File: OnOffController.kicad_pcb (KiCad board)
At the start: 2 copper layers, 16.3 x 26.4 mm, 35 parts, among them J1 S2B-PH-K-SLFSN, J2 Conn_01x02_Pin, J3 Conn_01x04_Pin, J4 Conn_01x04_Pin, J8 47589-0001, SW1 KMR211GLFS, U1 STM6601, U2 MCP73831-2-OT, U3 SPX3819M5-L

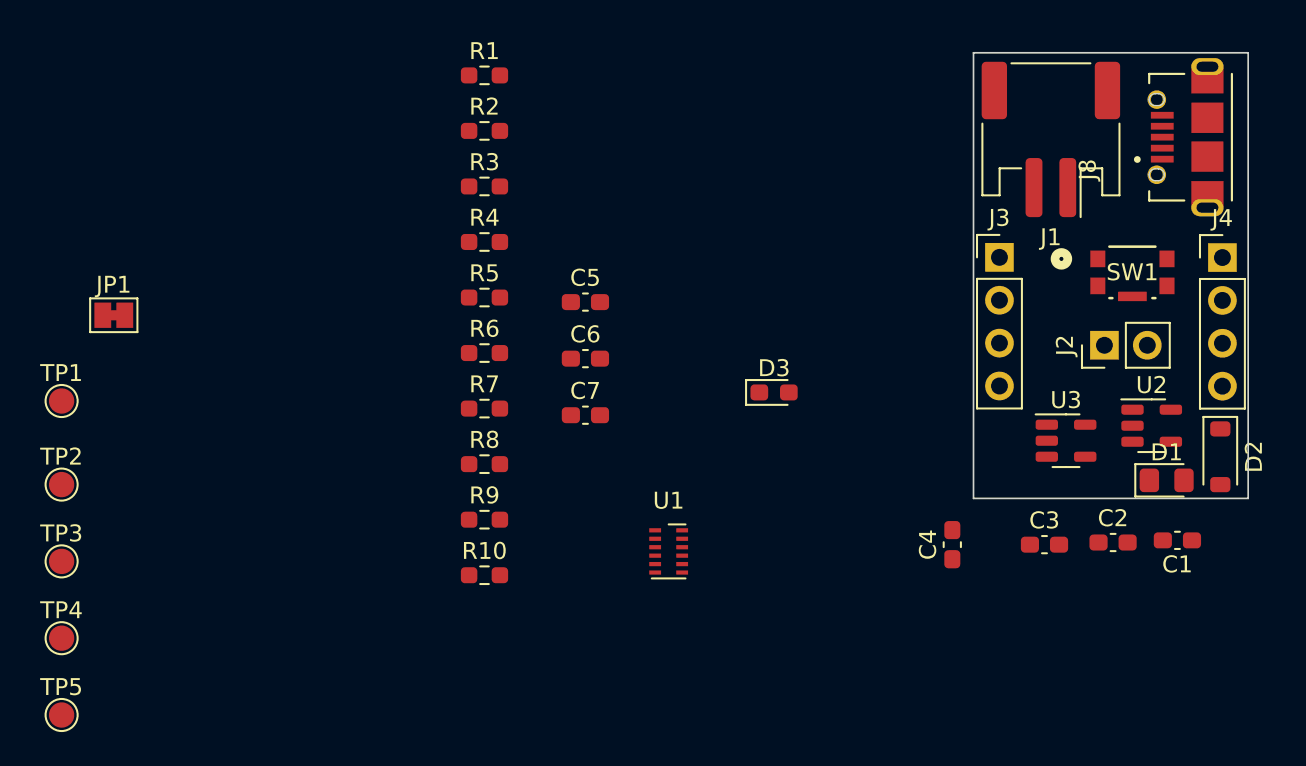
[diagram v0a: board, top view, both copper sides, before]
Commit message: Passing DRC and added all silk screens
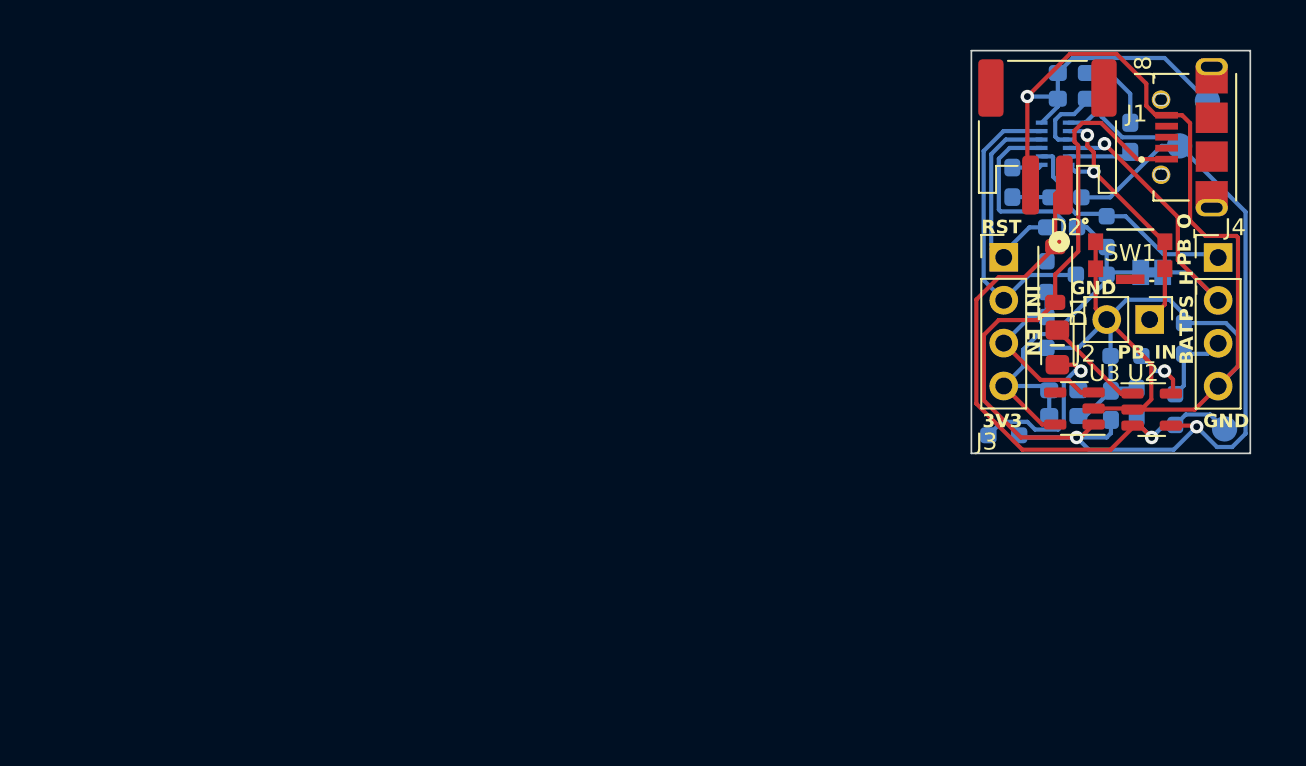
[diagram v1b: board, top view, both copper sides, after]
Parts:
- removed TP1, TP3: TestPoint, TestPoint:TestPoint_Pad_D1.5mm
- C1, C2, C3, C4, C5, C6, C7, D3, JP1, R1, R10, R2, R3, R4, R5, R6, R7, R8, R9, TP2, TP4, TP5, U1: moved to B.Cu
- moved TP4 72.4 mm to (164.1, 78.9), turned to 180 degrees
- moved TP2 71.6 mm to (165.7, 76.2), turned to 180 degrees
- moved TP5 70.9 mm to (166.8, 95.6), turned to 180 degrees
- moved JP1 61.5 mm to (162.4, 86.4), turned to 180 degrees
- moved R3 43.0 mm to (163.8, 94.5), turned to 90 degrees
- moved R4 41.8 mm to (164.3, 90.3), turned to 90 degrees
- moved R2 40.3 mm to (160.9, 91.3)
- moved R9 39.4 mm to (157.4, 81.9), turned to 180 degrees
- moved R1 37.4 mm to (153.7, 96.0)
- moved R5 37.1 mm to (159.8, 83.9), turned to 90 degrees
- moved R7 36.8 mm to (158.9, 86.5), turned to 180 degrees
- moved R10 36.3 mm to (156.2, 89.9), turned to -90 degrees
- moved C7 35.3 mm to (157.7, 74.5), turned to 180 degrees
- moved R8 35.1 mm to (156.2, 86.6), turned to -90 degrees
- moved R6 35.0 mm to (157.1, 83.7), turned to 180 degrees
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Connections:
- J3 pad 1: +3V3 -> /RST
- J3 pad 3: /RST -> /EN_DIV
- J3 pad 4: /EN_DIV -> +3V3
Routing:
- net GND: track 0.00 -> 105.2 mm, vias 0 -> 1
- net VBUS: track 0.00 -> 90.4 mm, vias 0 -> 2
- net VDC: track 0.00 -> 35.7 mm, vias 0 -> 1
- net +3V3: track 0.00 -> 23.9 mm
- net /PS_HOLD: track 0.00 -> 18.3 mm, vias 0 -> 1
- net /INT: track 0.00 -> 18.2 mm
- net Net-(J2-Pin_1): track 0.00 -> 16.0 mm, vias 0 -> 2
- net /RST: track 0.00 -> 14.0 mm
- net /PB_OUT: track 0.00 -> 13.8 mm
- net /EN: track 0.00 -> 12.7 mm
- net /EN_DIV: track 0.00 -> 11.2 mm
- net Net-(D1-A): track 0.00 -> 10.4 mm, vias 0 -> 1
- net Net-(D1-K): track 0.00 -> 6.13 mm
- net /BAT_SENSE: track 0.00 -> 4.89 mm
- net /Vref: track 0.00 -> 4.35 mm
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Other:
- board size 16.3 x 26.4 mm -> 16.5 x 23.9 mm
- board text added: "3V3"
- board text added: "BAT"
- board text added: "EN"
- board text added: "GND"
- board text added: "INT"
- board text added: "PB_IN"
- board text added: "PB_O"
- board text added: "PS_H"
- board text added: "RST"
- board text added: "VBUS"

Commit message: Added BOM
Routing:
- added copper zone on B.Cu, net GND
- added copper zone on F.Cu, net GND
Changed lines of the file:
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@@
   (segment (start 157.518 78.99) (end 159.389 78.99) (width 0.25) (layer "B.Cu") (net 28))
   (segment (start 159.389 78.99) (end 159.639 78.74) (width 0.25) (layer "B.Cu") (net 28))
+  (zone (net 2) (net_name "GND") (layers "F&B.Cu") (hatch edge 0.5)
+    (connect_pads (clearance 0.5))
+    (min_thickness 0.25) (filled_areas_thickness no)
+    (fill yes (thermal_gap 0.5) (thermal_bridge_width 0.5))
+    (polygon
+      (pts
+        (xy 151.765 73.279)
+        (xy 168.275 73.279)
+        (xy 168.275 97.028)
+        (xy 151.765 97.028)
+      )
+    )
+  )
 )

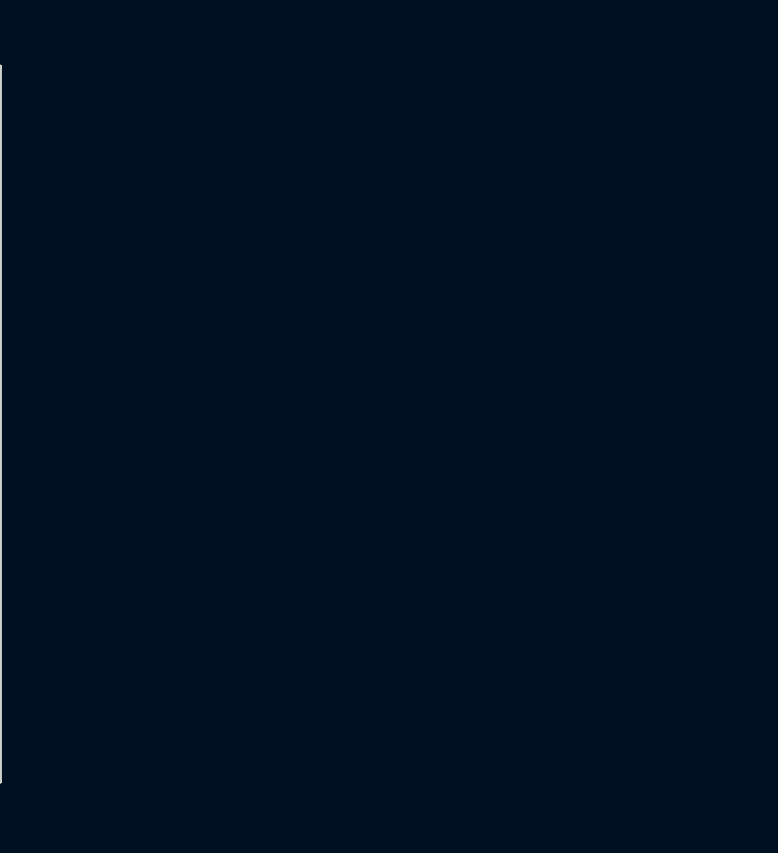
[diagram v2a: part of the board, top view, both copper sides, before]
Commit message: Updated all parts to smaller package sizes and found cheaper alternatives
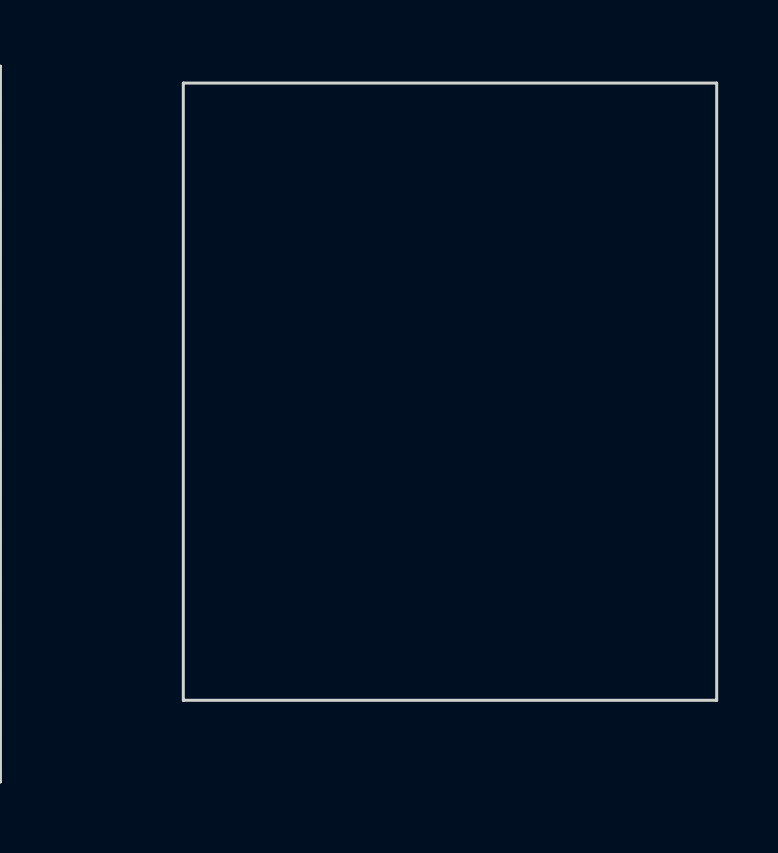
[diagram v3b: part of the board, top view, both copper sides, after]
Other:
- board size 16.5 x 23.9 mm -> 40.4 x 23.9 mm

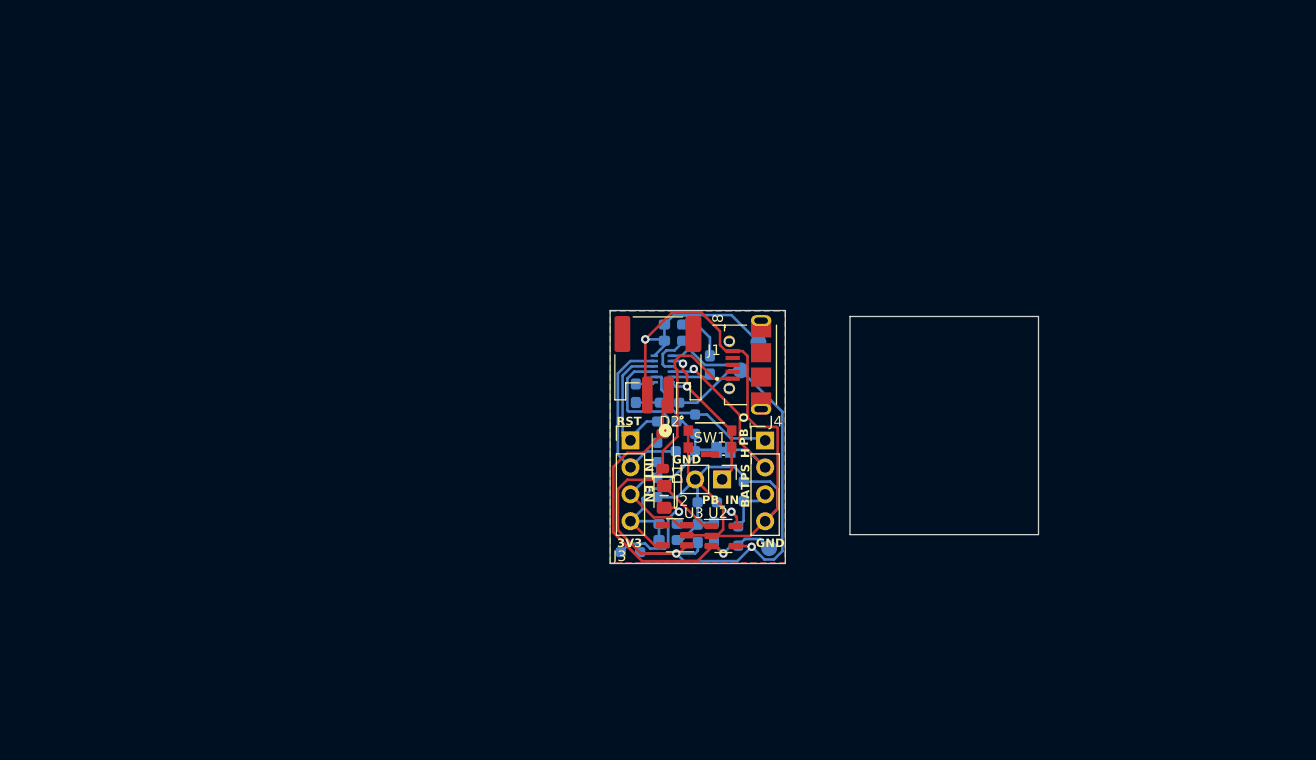
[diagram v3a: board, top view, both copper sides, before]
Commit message: Updated to 5V and 3.3V versions
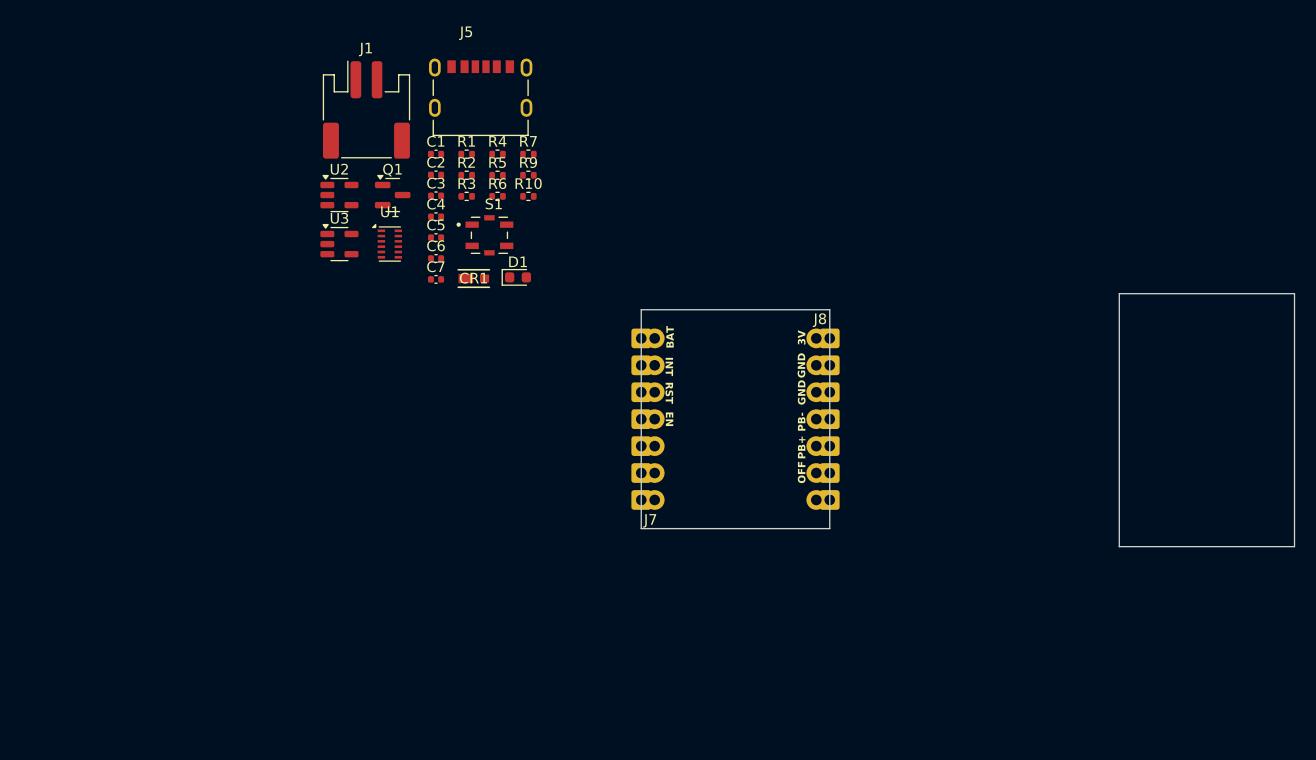
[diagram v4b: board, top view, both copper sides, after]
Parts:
- removed D2: MBR0520, Diode_SMD:D_SOD-123
- removed D3: LED, LED_SMD:LED_0603_1608Metric_Pad1.05x0.95mm_HandSolder
- removed J2: Conn_01x02_Pin, Connector_PinHeader_2.54mm:PinHeader_1x02_P2.54mm_Vertical
- removed J3, J4: Conn_01x04_Pin, Connector_PinHeader_2.54mm:PinHeader_1x04_P2.54mm_Vertical
- removed JP1: SolderJumper_2_Bridged, Jumper:SolderJumper-2_P1.3mm_Bridged_Pad1.0x1.5mm
- removed R8: 3.48K, Resistor_SMD:R_0603_1608Metric_Pad0.98x0.95mm_HandSolder
- removed SW1: KMR211GLFS, KMR2_Switch:KMR2xxG_CNK
- removed TP2, TP4, TP5: TestPoint, TestPoint:TestPoint_Pad_D1.5mm
- added CR1: MSS2P2-M3/89A, MSS2P2-M3:DIODE_MSP3V3, F.Cu at (138.9, 70.2)
- added J5: UJC-H-G-SMT-P6-TR, UJC-H-G-SMT-P6-TR:SAMESKY_UJC-H-G-SMT-P6-TR, F.Cu at (139.5, 54.1)
- added J7: Conn_01x07_Pin, Connector_PinHeader_2.54mm:qtpy_catellated_7x2, F.Cu at (154.7, 93.6)
- added Q1: MMBT3904, Package_TO_SOT_SMD:SOT-23, F.Cu at (131.2, 62.3)
- added S1: TS21-34-035-BK-260-SMT-TR, TS21_34_035_BK_260:SW_TS21-34-035-BK-260-SMT-TR, F.Cu at (140.4, 66.1)
- C1, C2, C3, C4, C5, C6, C7: footprint Capacitor_SMD:C_0603_1608Metric_Pad1.08x0.95mm_HandSolder -> Capacitor_SMD:C_0402_1005Metric; moved to F.Cu
- D1: footprint LED_SMD:LED_0805_2012Metric_Pad1.15x1.40mm_HandSolder -> LED_SMD:LED_0603_1608Metric
- J8: value 47589-0001 -> Conn_01x07_Pin; footprint 47589_0001_USB_B:MOLEX_47589-0001 -> Connector_PinHeader_2.54mm:qtpy_catellated_7x2
- R1, R2, R3, R4, R5, R6, R7, R9: footprint Resistor_SMD:R_0603_1608Metric_Pad0.98x0.95mm_HandSolder -> Resistor_SMD:R_0402_1005Metric; moved to F.Cu
- R10: value 10K -> 1K; footprint Resistor_SMD:R_0603_1608Metric_Pad0.98x0.95mm_HandSolder -> Resistor_SMD:R_0402_1005Metric; moved to F.Cu
- U1: moved to F.Cu
- moved U2 48.4 mm to (126.2, 62.3)
- moved C1 44.2 mm to (135.3, 58.5), turned to 0 degrees
- moved U3 41.9 mm to (126.2, 67.0), turned to 0 degrees
- moved C2 41.9 mm to (135.3, 60.4), turned to 0 degrees
- moved R3 41.0 mm to (138.2, 62.5), turned to 0 degrees
- moved R1 40.6 mm to (138.2, 58.5)
- moved R4 39.4 mm to (141.1, 58.5), turned to 0 degrees
- moved C3 39.2 mm to (135.3, 62.4)
- moved R2 38.3 mm to (138.2, 60.5)
- moved J1 36.5 mm to (128.8, 54.3), turned to 0 degrees
- moved C4 36.3 mm to (135.3, 64.4)
- moved R7 31.7 mm to (144.0, 58.5), turned to 0 degrees
- moved R10 30.0 mm to (144.0, 62.5), turned to 0 degrees
- moved R5 30.0 mm to (141.1, 60.5), turned to 0 degrees
- moved U1 28.3 mm to (131.0, 67.0), turned to 0 degrees
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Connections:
- net /INT renamed /PB_Interrupt
- net /PB_OUT renamed /PB_Out_Raw
- J8 pad 1: VBUS -> +3V3
- J8 pad 2: unconnected-(J8-D--Pad2) -> GND
- J8 pad 3: unconnected-(J8-D+-Pad3) -> GND
- J8 pad 4: unconnected-(J8-ID-Pad4) -> GND
- R10 pad 1: /EN_DIV -> /Force_Shtdwn
- R10 pad 2: GND -> Net-(Q1-B)
- R9 pad 2: Net-(D3-A) -> Net-(U1-~{VCC}_LO)
- U1 pad 2: Net-(J2-Pin_1) -> /Switch_HighSide
- U1 pad 4: /PS_HOLD -> +3V3
- U1 pad 6: Net-(J2-Pin_1) -> /Switch_HighSide
- U1 pad 7: Net-(D3-K) -> Net-(U1-~{VCC}_LO)
- U3 pad 3: /EN_DIV -> /EN
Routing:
- net GND: track 105.2 -> 1.70 mm, vias 1 -> 0
- net VBUS: track 90.4 -> 0.00 mm, vias 2 -> 0
- net VDC: track 35.7 -> 0.00 mm, vias 1 -> 0
- net +3V3: track 23.9 -> 0.00 mm
- net /PS_HOLD: track 18.3 -> 0.00 mm, vias 1 -> 0
- net /PB_Interrupt: track 18.2 -> 0.87 mm
- net Net-(J2-Pin_1): track 16.0 -> 0.00 mm, vias 2 -> 0
- net /RST: track 14.0 -> 0.16 mm
- net /PB_Out_Raw: track 13.8 -> 0.12 mm
- net /EN: track 12.7 -> 0.58 mm
- net /EN_DIV: track 11.2 -> 0.00 mm
- net Net-(D1-A): track 10.4 -> 0.00 mm, vias 1 -> 0
- net Net-(D1-K): track 6.13 -> 0.00 mm
- net /Vref: track 4.35 -> 0.00 mm
- net Net-(U1-C_SRD): track 3.76 -> 0.00 mm
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- removed copper zone on B.Cu, net GND
- removed copper zone on F.Cu, net GND
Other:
- board size 40.4 x 23.9 mm -> 61.6 x 23.9 mm
- board text added: "3V"
- board text added: "OFF"
- board text added: "PB+"
- board text added: "PB-"
- board text removed: "3V3"
- board text removed: "PB_IN"
- board text removed: "PB_O"
- board text removed: "PS_H"
- board text removed: "VBUS"

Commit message: Split 3.3 and 5V into different board versions
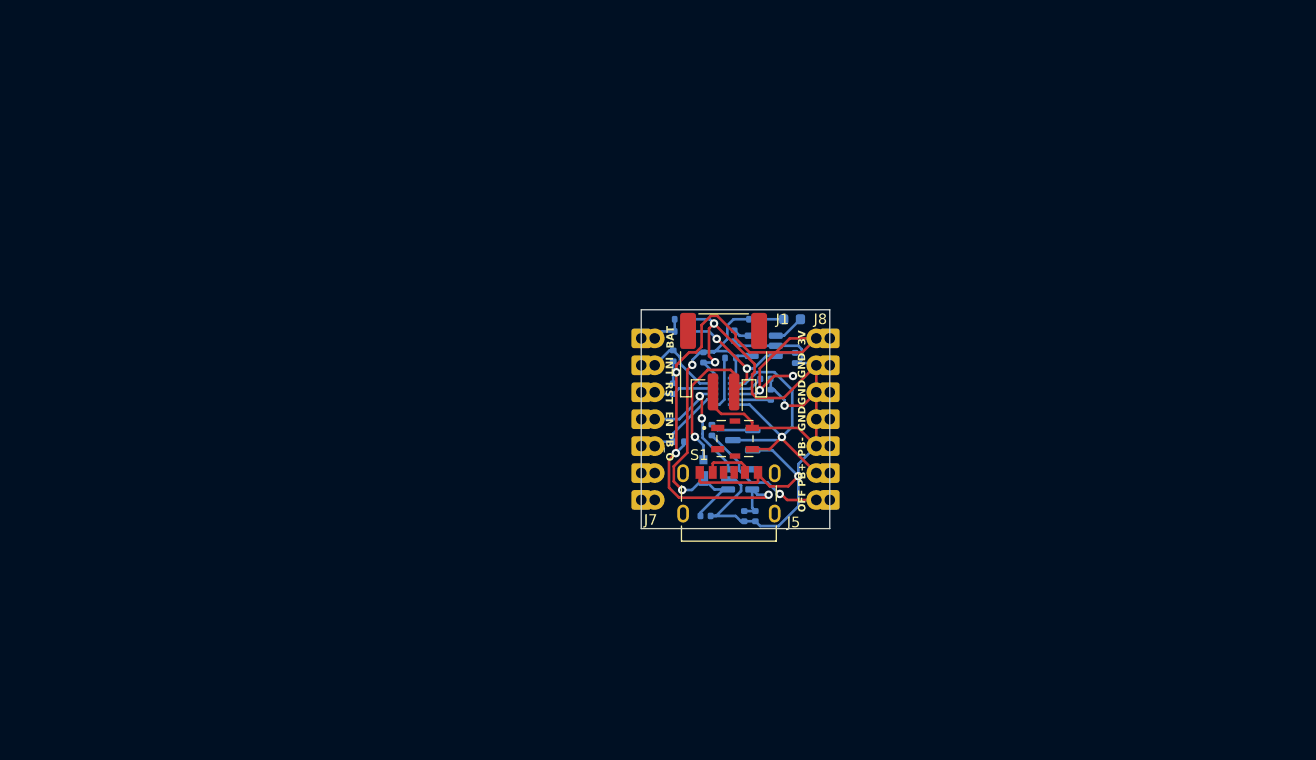
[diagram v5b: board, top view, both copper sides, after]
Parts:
- C1, C2, C3, C4, C5, C6, C7, CR1, D1, Q1, R1, R10, R2, R3, R4, R5, R6, R7, R9, U1, U2, U3: moved to B.Cu
- moved J5 44.9 mm to (162.9, 92.4)
- moved U3 43.8 mm to (164.0, 89.2)
- moved U2 42.5 mm to (166.2, 76.5), turned to 180 degrees
- moved C3 41.9 mm to (164.4, 92.6), turned to -90 degrees
- moved C4 41.3 mm to (165.4, 92.6), turned to -90 degrees
- moved J1 41.2 mm to (162.4, 78.0), turned to 180 degrees
- moved C2 41.0 mm to (160.8, 92.6)
- moved Q1 40.3 mm to (164.3, 85.5), turned to 180 degrees
- moved C1 38.9 mm to (169.2, 77.7), turned to -90 degrees
- moved U1 34.4 mm to (162.4, 80.8), turned to 180 degrees
- moved C6 34.1 mm to (166.9, 81.2), turned to 90 degrees
- moved C5 33.8 mm to (166.4, 79.7)
- moved R1 31.3 mm to (165.3, 74.0), turned to 180 degrees
- moved R5 30.4 mm to (158.2, 85.6), turned to 180 degrees
- moved S1 30.1 mm to (163.5, 85.3)
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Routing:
- net GND: track 1.70 -> 106.0 mm, vias 0 -> 4
- net +3V3: track 0.00 -> 65.2 mm, vias 0 -> 5
- net VBUS: track 0.00 -> 41.7 mm, vias 0 -> 2
- net /Switch_HighSide: track 0.00 -> 30.5 mm, vias 0 -> 1
- net VDC: track 0.00 -> 29.3 mm, vias 0 -> 3
- net /EN: track 0.58 -> 16.5 mm, vias 0 -> 2
- net /Force_Shtdwn: track 0.12 -> 12.9 mm, vias 0 -> 1
- net /PB_Out_Raw: track 0.12 -> 9.19 mm
- net /PB_Interrupt: track 0.87 -> 9.58 mm
- net /RST: track 0.16 -> 7.15 mm
- net Net-(U1-~{VCC}_LO): track 0.00 -> 5.07 mm
- net /BAT_SENSE: track 1.14 -> 5.59 mm
- net Net-(Q1-B): track 0.00 -> 4.06 mm
- net Net-(U1-C_SRD): track 0.00 -> 3.72 mm
- net /Vref: track 0.00 -> 3.11 mm
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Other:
- board size 61.6 x 23.9 mm -> 17.8 x 20.6 mm
- board text added: "PB_O"
